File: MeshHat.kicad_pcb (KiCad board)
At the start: 2 copper layers, 65 x 56.5 mm, 26 parts, among them J1 RPi_GPIO, U5 RP2040, U6 W25Q128JVS, U7 E22-900M30S, Y1 ABM8-272-T3

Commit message: place all components
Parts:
- added P1: USB_C_Plug_USB2.0, Connector_USB:USB_C_Receptacle_GCT_USB4110, F.Cu at (169.0, 103.1)
- added R8: 10k, Resistor_SMD:R_0402_1005Metric, F.Cu at (183.6, 92.4)
- added R9: 5K1, Resistor_SMD:R_0603_1608Metric, F.Cu at (167.6, 96.6)
- added SW1: SW_SPST, Button_Switch_SMD:SW_Push_1P1T_NO_CK_KMR2, F.Cu at (191.6, 102.2)
- added SW2: SW_SPST, Button_Switch_SMD:SW_Push_1P1T_NO_CK_KMR2, F.Cu at (169.1, 77.0)
- added U1: 24LC256, Package_SO:SOIC-8_5.3x5.3mm_P1.27mm, F.Cu at (178.2, 60.5)
- moved C1 113.4 mm to (184.3, 87.2)
- moved C9 107.0 mm to (184.3, 82.8)
- moved C4 106.8 mm to (183.3, 77.8)
- moved C6 105.9 mm to (178.8, 93.6), turned to -90 degrees
- moved R3 102.5 mm to (179.2, 89.7), turned to 90 degrees
- moved C2 102.1 mm to (178.2, 73.2), turned to 180 degrees
- moved C12 101.7 mm to (177.2, 93.6), turned to -90 degrees
- moved C5 100.9 mm to (172.3, 93.6), turned to -90 degrees
- moved R6 97.6 mm to (175.5, 93.6), turned to 90 degrees
- moved C3 97.5 mm to (174.2, 73.2), turned to 180 degrees
- moved R5 97.3 mm to (173.9, 93.6), turned to 90 degrees
- moved R4 95.6 mm to (178.3, 76.8), turned to 90 degrees
- moved R2 94.2 mm to (187.0, 61.0), turned to 90 degrees
- moved C13 92.8 mm to (174.4, 76.8), turned to 90 degrees
- moved C8 92.4 mm to (167.2, 83.0), turned to 180 degrees
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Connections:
- C3 pad 1: Net-(C3-Pad1) -> /MeshRF/R_X_IN
- R4 pad 1: GND -> /MeshRF/R_X_OUT
- R4 pad 2: /MeshRF/R_X_OUT -> Net-(C2-Pad2)
- U5 pad 20: GND -> /MeshRF/R_X_IN
- Y1 pad 1: Net-(C3-Pad1) -> /MeshRF/R_X_IN

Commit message: more of the layout
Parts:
- removed P1: USB_C_Plug_USB2.0, Connector_USB:USB_C_Receptacle_GCT_USB4110
- added J2: USB_B_Mini, Connector_USB:USB_Mini-B_Lumberg_2486_01_Horizontal, F.Cu at (171.0, 100.4)
- moved C2 3.90 mm to (174.3, 73.2), turned to 0 degrees
- moved C3 3.74 mm to (177.9, 73.2), turned to 0 degrees
- moved C7 3.30 mm to (167.2, 88.0)
- moved C11 1.75 mm to (167.2, 86.3)
- moved C10 1.71 mm to (167.2, 84.7)
- moved SW1 1.31 mm to (190.4, 102.6)
- moved U6 1.31 mm to (182.2, 100.2)
- turned Y1 to 180 degrees
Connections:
- U5 pad 11: unconnected-(U5-GPIO8-Pad11) -> /MeshRF/RF_NSS
- U5 pad 12: unconnected-(U5-GPIO9-Pad12) -> /MeshRF/RF_DIO2
- U5 pad 13: unconnected-(U5-GPIO10-Pad13) -> /MeshRF/RF_TXEN
- U5 pad 14: unconnected-(U5-GPIO11-Pad14) -> /MeshRF/RF_RXEN
- U5 pad 4: unconnected-(U5-GPIO2-Pad4) -> /MeshRF/RF_DIO1
- U5 pad 5: unconnected-(U5-GPIO3-Pad5) -> /MeshRF/RF_BUSY
- U5 pad 6: unconnected-(U5-GPIO4-Pad6) -> /MeshRF/~{RF_RST}
- U5 pad 7: unconnected-(U5-GPIO5-Pad7) -> /MeshRF/RF_MISO
- U5 pad 8: unconnected-(U5-GPIO6-Pad8) -> /MeshRF/RF_MOSI
- U5 pad 9: unconnected-(U5-GPIO7-Pad9) -> /MeshRF/RF_SCK

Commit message: route more of the layout
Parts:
- removed R8: 10k, Resistor_SMD:R_0402_1005Metric
- removed R9: 5K1, Resistor_SMD:R_0603_1608Metric
- added C15: 0U1, Capacitor_SMD:C_0603_1608Metric, F.Cu at (175.6, 93.6)
- J1: footprint RPi_HAT:RPI_Hat_B+ -> RPi Hat:RPI_Hat_B+
- U1: footprint Package_SO:SOIC-8_5.3x5.3mm_P1.27mm -> Package_SO:TSSOP-8_4.4x3mm_P0.65mm
- moved R3 19.0 mm to (191.8, 103.9), turned to 180 degrees
- moved C13 12.9 mm to (164.4, 85.0)
- moved C4 8.54 mm to (174.8, 76.9), turned to 90 degrees
- moved U1 7.71 mm to (184.6, 64.9), turned to 90 degrees
- moved SW1 6.48 mm to (196.8, 103.0)
- moved C11 4.10 mm to (169.6, 89.7)
- moved R2 3.28 mm to (184.3, 59.1), turned to -90 degrees
- moved U6 3.17 mm to (184.7, 102.2)
- moved C10 2.81 mm to (169.6, 86.2)
- moved R1 2.59 mm to (186.2, 59.1), turned to -90 degrees
- moved C7 2.37 mm to (169.6, 88.0)
- moved C8 2.36 mm to (169.6, 83.0)
- moved C5 1.90 mm to (170.4, 93.6)
- moved SW2 1.87 mm to (169.4, 78.8)
- moved R5 1.80 mm to (172.1, 93.6)
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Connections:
- SW1 pad 2: /MeshRF/R_USB_ BOOT -> R_USB_BOOT
- U1 pad 5: /EEPROM_SDA -> /E_SDA
- U1 pad 6: /EEPROM_I2C -> /E_I2C
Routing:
- net /MeshRF/RF_DIO1: track 0.00 -> 40.8 mm, vias 0 -> 2
- net /MeshRF/RF_NSS: track 0.00 -> 39.3 mm, vias 0 -> 2
- net /MeshRF/RF_BUSY: track 0.00 -> 39.2 mm, vias 0 -> 2
- net /MeshRF/RF_SCK: track 0.00 -> 38.4 mm, vias 0 -> 2
- net /MeshRF/~{RF_RST}: track 0.00 -> 38.3 mm, vias 0 -> 2
- net /MeshRF/RF_MOSI: track 0.00 -> 37.8 mm, vias 0 -> 2
- net /MeshRF/RF_MISO: track 0.00 -> 37.6 mm, vias 0 -> 2
- net R_SWCLK: track 0.00 -> 31.4 mm, vias 0 -> 1
- net +3.3V: track 0.00 -> 31.3 mm
- net GND: track 0.00 -> 29.9 mm, vias 0 -> 24
- net R_SWDIO: track 0.00 -> 29.7 mm, vias 0 -> 1
- net +1V1: track 0.00 -> 27.3 mm, vias 0 -> 2
- net /MeshRF/~{F_SS}: track 0.00 -> 26.3 mm
- net /MeshRF/F_SD1: track 0.00 -> 23.8 mm
- net /MeshRF/F_SD2: track 0.00 -> 18.6 mm
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- added copper zone on F.Cu, net +3.3V
- added copper zone on B.Cu, net GND
- added copper zone on F.Cu, net GND
- added copper zone on In1.Cu, net GND
- added copper zone on In2.Cu, net GND
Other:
- copper layers 2 -> 4
- board text added: "${REFERENCE}"

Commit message: more cleanup of the schematic
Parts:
- added R8: 10k, Resistor_SMD:R_0402_1005Metric, F.Cu at (123.5, 82.5)
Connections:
- U5 pad 11: /MeshRF/RF_NSS -> /MeshRF/RF_DIO2
- U5 pad 12: /MeshRF/RF_DIO2 -> /MeshRF/RF_TXEN
- U5 pad 13: /MeshRF/RF_TXEN -> /MeshRF/RF_RXEN
- U5 pad 14: /MeshRF/RF_RXEN -> unconnected-(U5-GPIO11-Pad14)
- U5 pad 3: unconnected-(U5-GPIO1-Pad3) -> /MeshRF/RF_DIO1
- U5 pad 4: /MeshRF/RF_DIO1 -> /MeshRF/RF_BUSY
- U5 pad 5: /MeshRF/RF_BUSY -> /MeshRF/~{RF_RST}
- U5 pad 6: /MeshRF/~{RF_RST} -> /MeshRF/RF_MISO
- U5 pad 7: /MeshRF/RF_MISO -> /MeshRF/RF_NSS
- U5 pad 8: /MeshRF/RF_MOSI -> /MeshRF/RF_SCK
- U5 pad 9: /MeshRF/RF_SCK -> /MeshRF/RF_MOSI
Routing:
- net /MeshRF/RF_SCK: track 38.4 -> 35.2 mm
- net /MeshRF/RF_MISO: track 37.6 -> 35.4 mm
- net /MeshRF/RF_NSS: track 39.3 -> 37.5 mm
- net /MeshRF/RF_MOSI: track 37.8 -> 36.1 mm
- net /MeshRF/~{RF_RST}: track 38.3 -> 36.6 mm
- net /MeshRF/RF_DIO1: track 40.8 -> 39.1 mm
- net /MeshRF/RF_DIO2: track 15.5 -> 13.9 mm
- net /MeshRF/RF_TXEN: track 13.2 -> 11.8 mm
- net /MeshRF/RF_RXEN: track 11.4 -> 10.3 mm

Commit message: WIP
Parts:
- added R9: 10K, Resistor_SMD:R_0603_1608Metric, F.Cu at (1.50, 0.76)
- moved R3 69.0 mm to (204.0, 36.0), turned to 0 degrees
- moved SW1 67.9 mm to (213.0, 37.0), turned to -90 degrees
- moved J2 53.5 mm to (210.8, 64.7), turned to 90 degrees
- moved C13 45.0 mm to (208.8, 77.5), turned to -90 degrees
- moved R7 42.9 mm to (207.9, 83.7), turned to 90 degrees
- moved U6 40.4 mm to (191.1, 62.3), turned to 0 degrees
- moved C5 39.9 mm to (203.6, 71.4), turned to 0 degrees
- moved C11 37.8 mm to (203.6, 73.2), turned to 0 degrees
- moved R5 37.0 mm to (201.1, 70.6), turned to -90 degrees
- moved C7 36.4 mm to (203.6, 75.0), turned to 0 degrees
- moved R1 35.6 mm to (197.5, 25.2)
- moved R2 35.6 mm to (195.6, 25.2)
- moved U7 35.6 mm to (166.4, 78.8), turned to 0 degrees
- moved C10 35.3 mm to (203.6, 76.8), turned to 0 degrees
- moved SW2 34.7 mm to (203.8, 83.7), turned to 180 degrees
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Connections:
- J1 pad 10: unconnected-(J1-BCM15_RXD-Pad10) -> R_RX
- J1 pad 29: /E_I2C -> unconnected-(J1-BCM5-Pad29)
- J1 pad 8: unconnected-(J1-BCM14_TXD-Pad8) -> R_TX
- R2 pad 2: /E_I2C -> /E_SCL
- U1 pad 6: /E_I2C -> /E_SCL
- U5 pad 15: unconnected-(U5-GPIO12-Pad15) -> R_RX
- U5 pad 16: unconnected-(U5-GPIO13-Pad16) -> R_TX
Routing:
- net /MeshRF/RF_DIO1: track 39.1 -> 0.00 mm, vias 2 -> 0
- net /MeshRF/RF_NSS: track 37.5 -> 1.65 mm, vias 2 -> 0
- net /MeshRF/RF_BUSY: track 38.8 -> 6.48 mm, vias 2 -> 0
- net /MeshRF/RF_SCK: track 35.2 -> 3.64 mm, vias 2 -> 0
- net /MeshRF/RF_MOSI: track 36.1 -> 9.57 mm, vias 2 -> 1
- net R_SWCLK: track 31.4 -> 6.35 mm
- net /MeshRF/~{RF_RST}: track 36.6 -> 15.7 mm, vias 2 -> 1
- net /MeshRF/RF_MISO: track 35.4 -> 14.8 mm, vias 2 -> 1
- net R_SWDIO: track 29.7 -> 10.8 mm
- net /E_I2C: track 17.5 -> 0.00 mm
- net /E_SCL: track 0.00 -> 13.9 mm
- net /MeshRF/RF_DIO2: track 13.9 -> 2.56 mm
- net /MeshRF/RF_TXEN: track 11.8 -> 2.31 mm
- net /MeshRF/RF_RXEN: track 10.3 -> 2.06 mm
- net /MeshRF/~{F_SS}: track 26.3 -> 19.5 mm
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- added copper zone on B.Cu, net +3.3V
- removed copper zone on F.Cu, net +3.3V
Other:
- outline, holes or cut-outs redrawn
- board text removed: "${REFERENCE}"

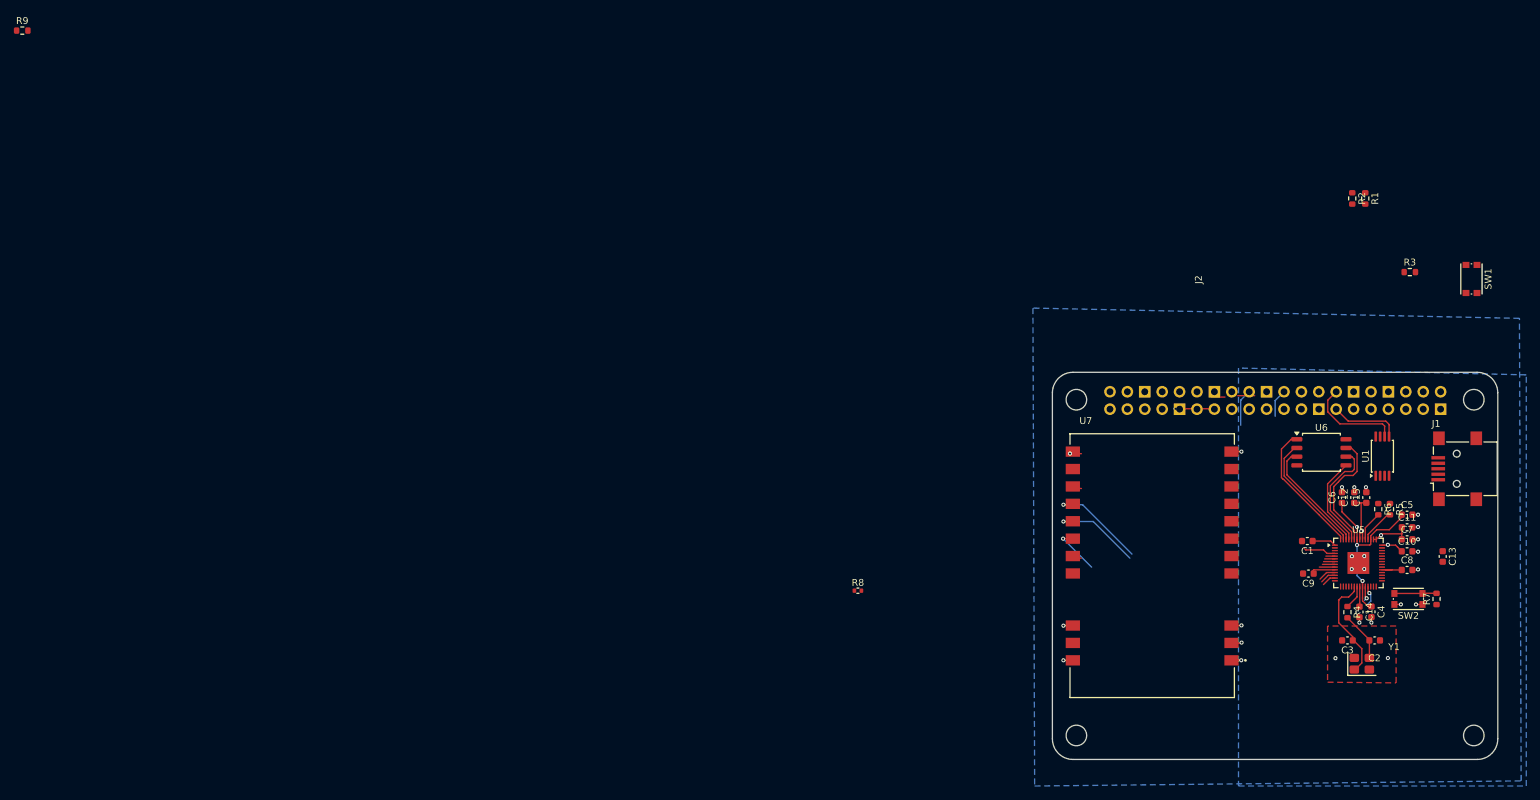
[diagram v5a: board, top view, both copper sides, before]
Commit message: add integration test arduino script
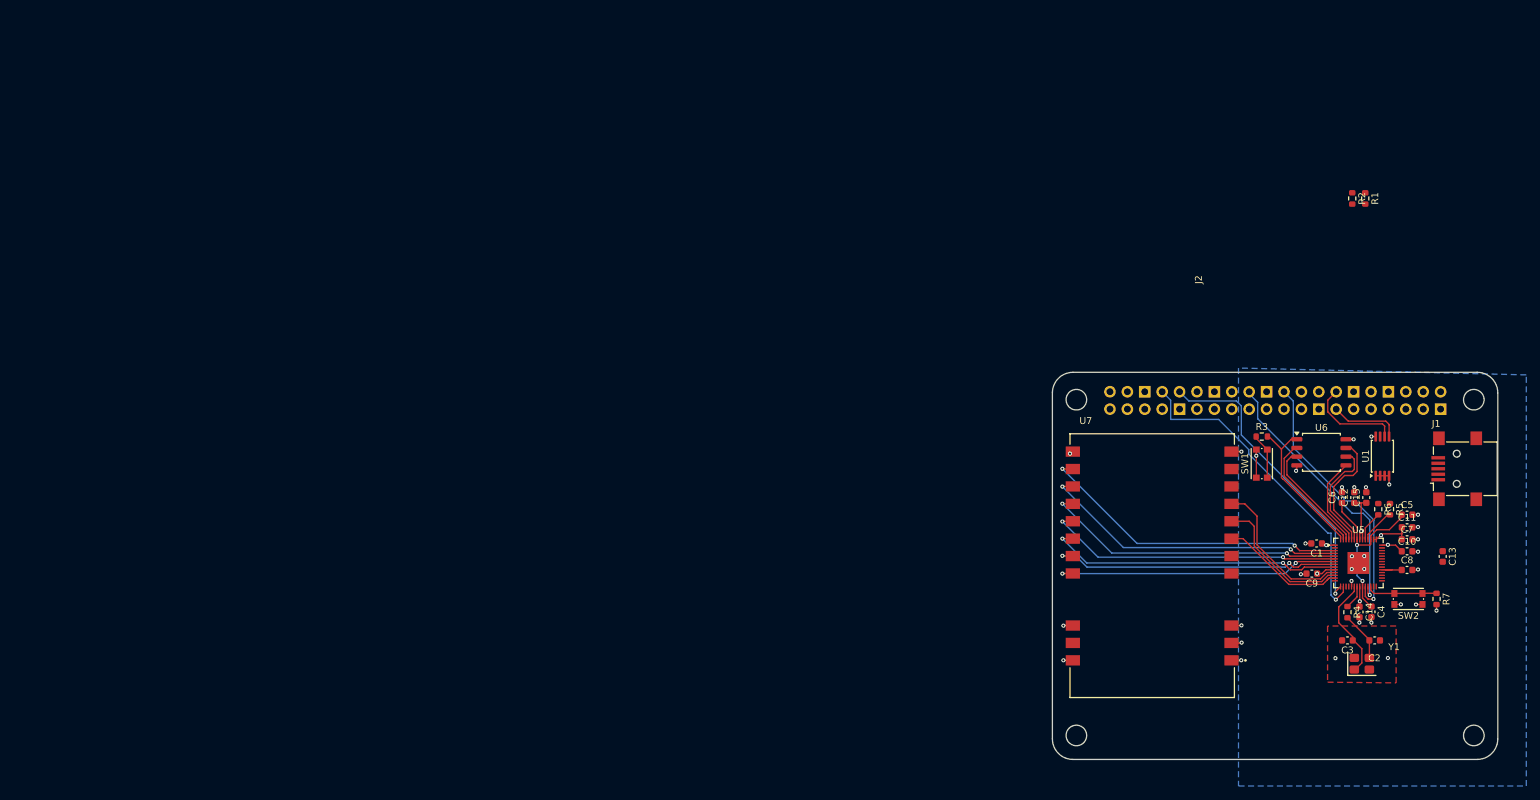
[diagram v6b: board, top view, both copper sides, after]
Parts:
- removed R8: 10k, Resistor_SMD:R_0402_1005Metric
- removed R9: 10K, Resistor_SMD:R_0603_1608Metric
- moved SW1 40.8 mm to (182.4, 64.0), turned to 90 degrees
- moved R3 32.3 mm to (182.4, 60.0)
- moved C1 1.40 mm to (190.4, 75.6)
- moved C9 0.50 mm to (189.7, 80.0)
- turned R7 to -90 degrees
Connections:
- R7 pad 1: +3.3V -> R_RUN
- R7 pad 2: R_RUN -> +3.3V
- U1 pad 8: +3V3 -> +3.3V
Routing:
- net R_TX: track 0.00 -> 47.6 mm, vias 0 -> 1
- net /MeshRF/RF_DIO1: track 0.00 -> 46.3 mm, vias 0 -> 2
- net R_RX: track 0.00 -> 44.3 mm, vias 0 -> 1
- net /MeshRF/RF_NSS: track 1.65 -> 42.1 mm, vias 0 -> 2
- net /MeshRF/RF_SCK: track 3.64 -> 42.6 mm, vias 0 -> 2
- net /MeshRF/RF_BUSY: track 6.48 -> 45.3 mm, vias 0 -> 2
- net /MeshRF/RF_MOSI: track 9.57 -> 43.6 mm, vias 1 -> 2
- net R_SWCLK: track 6.35 -> 39.4 mm
- net /MeshRF/RF_MISO: track 14.8 -> 43.8 mm, vias 1 -> 2
- net /MeshRF/~{RF_RST}: track 15.7 -> 44.5 mm, vias 1 -> 2
- net R_SWDIO: track 10.8 -> 38.9 mm
- net /MeshRF/RF_DIO2: track 2.56 -> 22.5 mm
- net /MeshRF/RF_TXEN: track 2.31 -> 20.8 mm
- net /MeshRF/RF_RXEN: track 2.06 -> 18.4 mm
- net R_USB_BOOT: track 0.00 -> 6.40 mm
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- removed copper zone on B.Cu, net GND

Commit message: get most of the changes in
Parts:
- removed U1: 24LC256, Package_SO:TSSOP-8_4.4x3mm_P0.65mm
- added C16: 0U1, Capacitor_SMD:C_0603_1608Metric, F.Cu at (198.0, 61.2)
- added C17: 1U, Capacitor_SMD:C_0603_1608Metric, F.Cu at (181.5, 66.9)
- added C18: 0U1, Capacitor_SMD:C_0603_1608Metric, F.Cu at (181.5, 65.1)
- added U3: CAT24C128, Package_SO:TSSOP-8_4.4x3mm_P0.65mm, F.Cu at (201.0, 62.9)
- moved R1 35.7 mm to (206.0, 59.4)
- moved R2 34.8 mm to (204.0, 59.4)
- moved C13 20.6 mm to (196.2, 61.2)
- moved R3 13.7 mm to (188.6, 72.2), turned to 90 degrees
- moved SW1 8.59 mm to (184.8, 72.2), turned to 0 degrees
- moved J2 2.80 mm to (210.8, 67.5)
- moved U6 0.85 mm to (190.2, 62.2)
- moved C1 0.70 mm to (189.7, 75.6)
- renumbered R2 to R1, R1 to R2
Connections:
- J1 pad 23: unconnected-(J1-BCM11_SCLK-Pad23) -> /E_WP
- R1 pad 1: +3V3 -> +3.3V
- R2 pad 1: +3V3 -> +3.3V
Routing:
- net +5V: track 0.00 -> 35.2 mm
- net /E_WP: track 0.00 -> 15.2 mm
- net GND: track 30.2 -> 41.4 mm, vias 31 -> 35
- net /E_SCL: track 13.9 -> 21.1 mm
- net R_RX: track 44.3 -> 38.5 mm
- net R_TX: track 47.6 -> 42.4 mm
- net +3.3V: track 32.1 -> 36.4 mm, vias 9 -> 11
- net /E_SDA: track 10.2 -> 13.3 mm
- net R_SWDIO: track 38.9 -> 38.0 mm
- net R_SWCLK: track 39.4 -> 38.5 mm
- net /MeshRF/F_SD1: track 17.6 -> 18.4 mm
- net /MeshRF/F_SD2: track 16.7 -> 17.5 mm
- net /MeshRF/~{F_SS}: track 22.1 -> 21.4 mm
- net R_USB_BOOT: track 6.40 -> 5.86 mm
- added copper zone on In2.Cu, net +3.3V
- added copper zone on F.Cu, net +5V
- removed copper zone on B.Cu, net +3.3V
- removed copper zone on In2.Cu, net GND

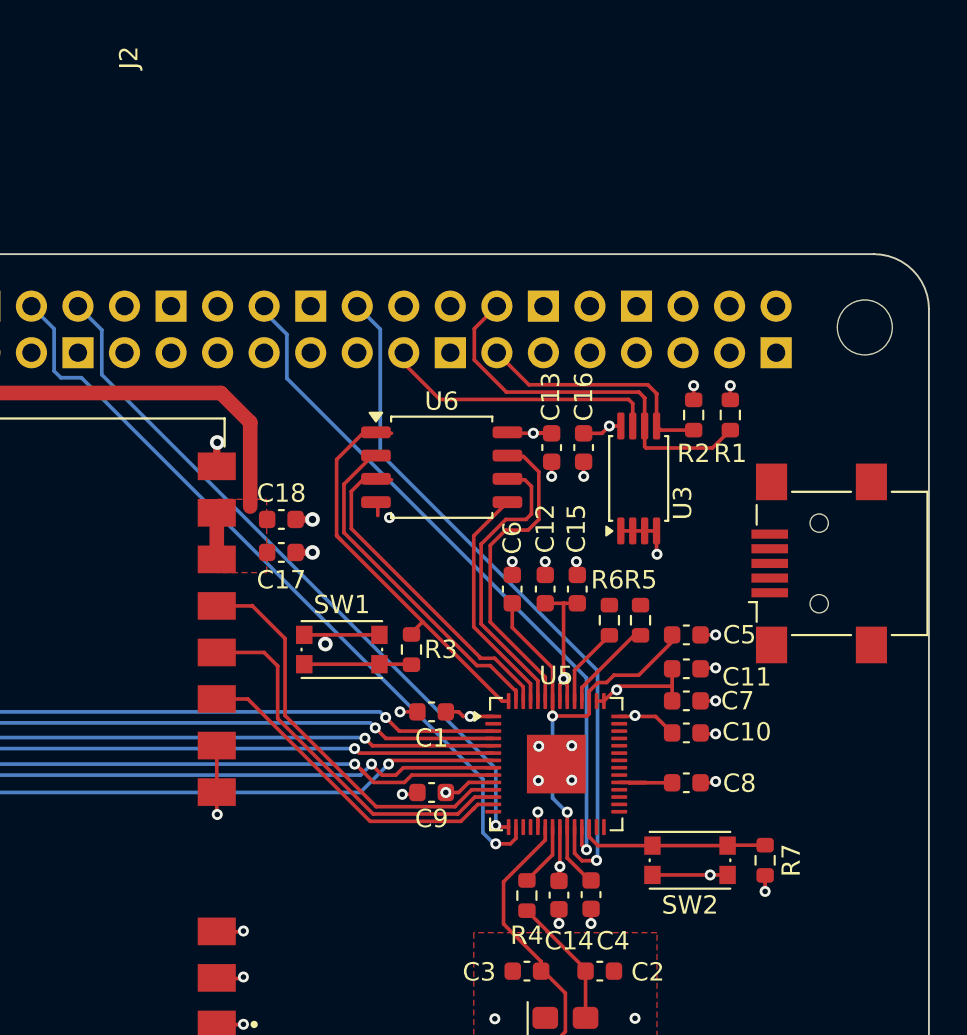
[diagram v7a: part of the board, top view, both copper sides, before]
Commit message: re-route the swdio lines
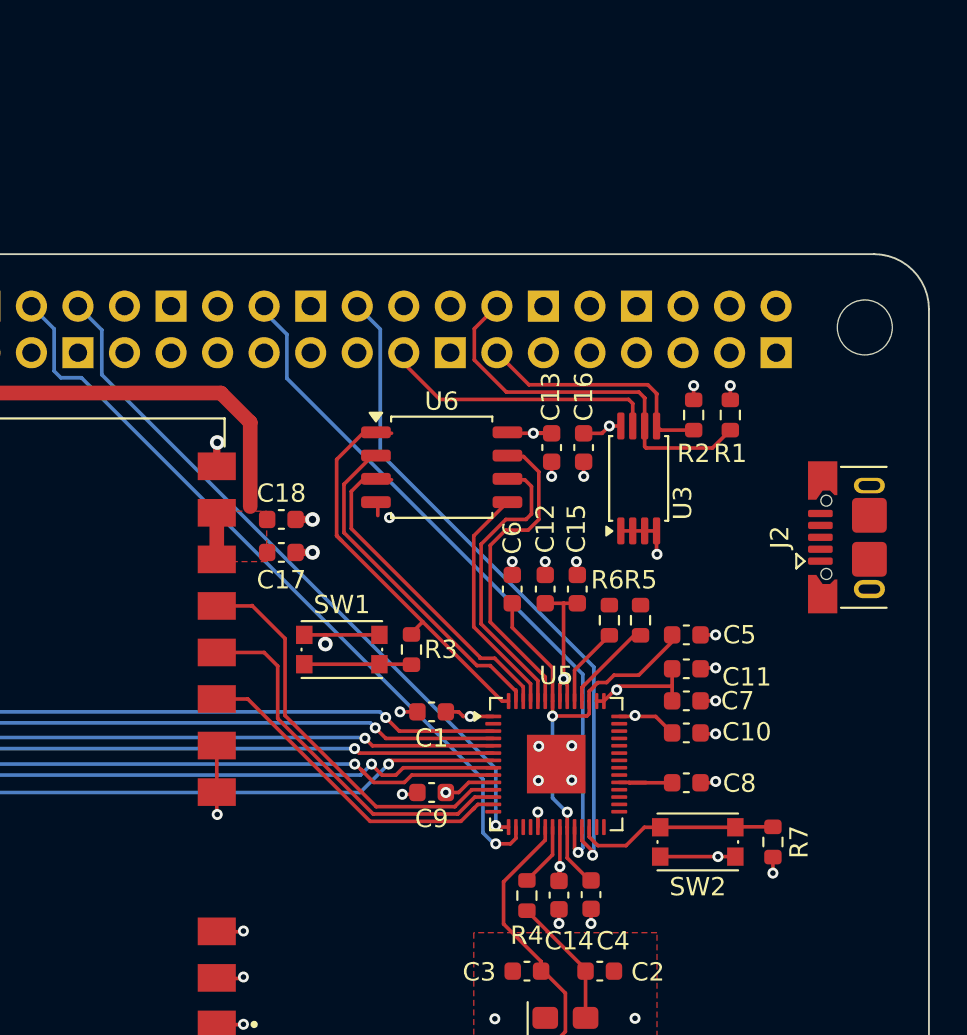
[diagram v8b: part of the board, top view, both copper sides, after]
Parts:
- J2: footprint Connector_USB:USB_Mini-B_Lumberg_2486_01_Horizontal -> Connector_USB:USB_Micro-B_XKB_U254-051T-4BH83-F1S
- moved J2 2.75 mm to (213.2, 66.1)
- moved R7 1.09 mm to (208.3, 82.7)
- moved SW2 1.09 mm to (204.2, 82.7)
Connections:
- J1 pad 18: R_SWDIO -> R_SWCLK
- J1 pad 22: R_SWCLK -> R_SWDIO
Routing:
- net R_SWDIO: track 38.0 -> 37.1 mm
- net R_RUN: track 10.3 -> 11.1 mm
